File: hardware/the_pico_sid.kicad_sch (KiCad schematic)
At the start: 17 parts, among them J1 SWD, J2 Conn_01x06, U1 LM324, U2 SID_6581, U3 Pico, U4 4050, U5 4050, U6 74HC245

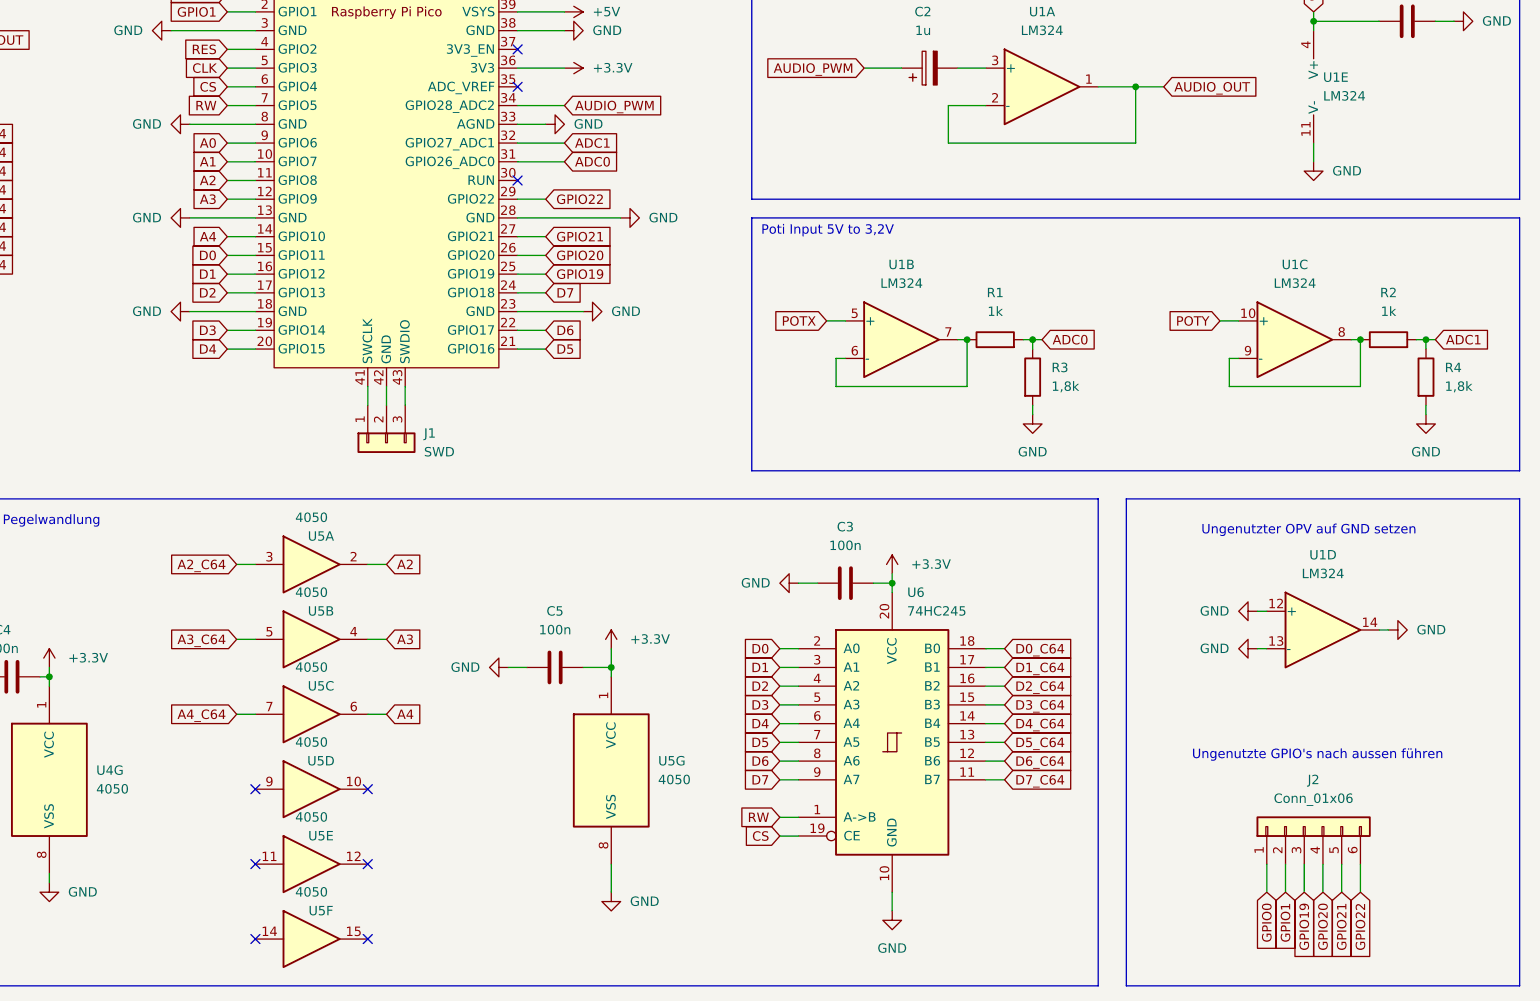
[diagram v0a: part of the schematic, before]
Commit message: schematic: changed the adc implementation
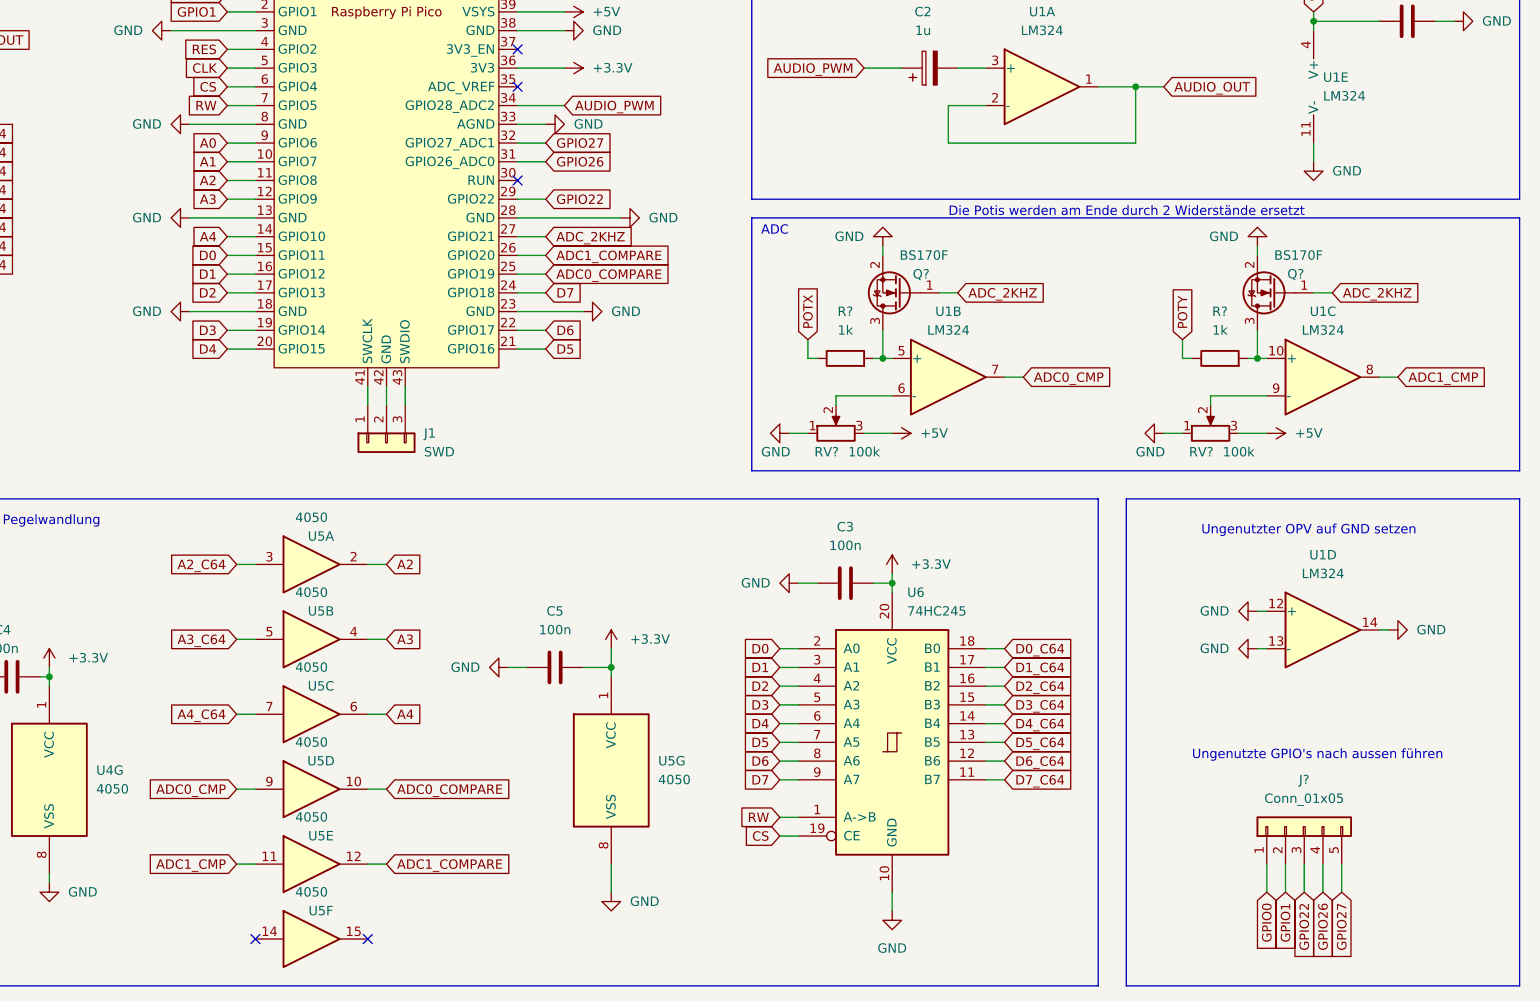
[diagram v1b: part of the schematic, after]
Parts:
- removed J2: Conn_01x06, symbol Connector_Generic:Conn_01x06
- removed R1, R2: 1k, symbol Device:R
- removed R3, R4: 1,8k, symbol Device:R
- added J?: Conn_01x05, symbol Connector_Generic:Conn_01x05
- added Q? (x2): BS170F, Package_TO_SOT_SMD:SOT-23, symbol Transistor_FET:BS170F
- added R? (x2): 1k, symbol Device:R
- added RV? (x2): 100k, symbol Device:R_Potentiometer
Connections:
- net GPIO19 is gone; now on net ADC0_COMPARE: U3.25 (GPIO19)
- net GPIO20 is gone; now on net ADC1_COMPARE: U3.26 (GPIO20)
- net +5V: now also RV?.3, RV?.3
- net GND: now also Q?.2 (S), Q?.2 (S), RV?.1, RV?.1
- net GPIO0: now also J?.1 (Pin_1)
- net GPIO1: now also J?.2 (Pin_2)
- net GPIO22: now also J?.3 (Pin_3)
- net POTX: now also R?.1; no longer U1.5 (+)
- net POTY: now also R?.1; no longer U1.10 (+)
- net ADC0_COMPARE: now reaches U5.10
- net ADC0_CMP: now reaches U5.9
- net ADC0_CMP: now also U1.7
- net at U1.6 (-): now also RV?.2; no longer U1.7
- net at U1.9 (-): now also RV?.2; no longer U1.8
- net ADC1_CMP: now reaches U5.11
- net ADC1_CMP: now also U1.8
- net ADC1_COMPARE: now reaches U5.12
- net ADC0 renamed GPIO26
- net GPIO26: now also J?.4 (Pin_4)
- net ADC1 renamed GPIO27
- net GPIO27: now also J?.5 (Pin_5)
- net GPIO21 renamed ADC_2KHZ
- net ADC_2KHZ: now also Q?.1 (G), Q?.1 (G)
- new net: Q?.3 (D), R?.2, U1.5 (+)
- new net: Q?.3 (D), R?.2, U1.10 (+)
- no-connect marks 15 -> 11
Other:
- note added: "ADC"
- note added: "Die Potis werden am Ende durch 2 Widerstände ersetzt"
- note removed: "Poti Input 5V to 3,2V"
- moved on the sheet: U1B, U1C

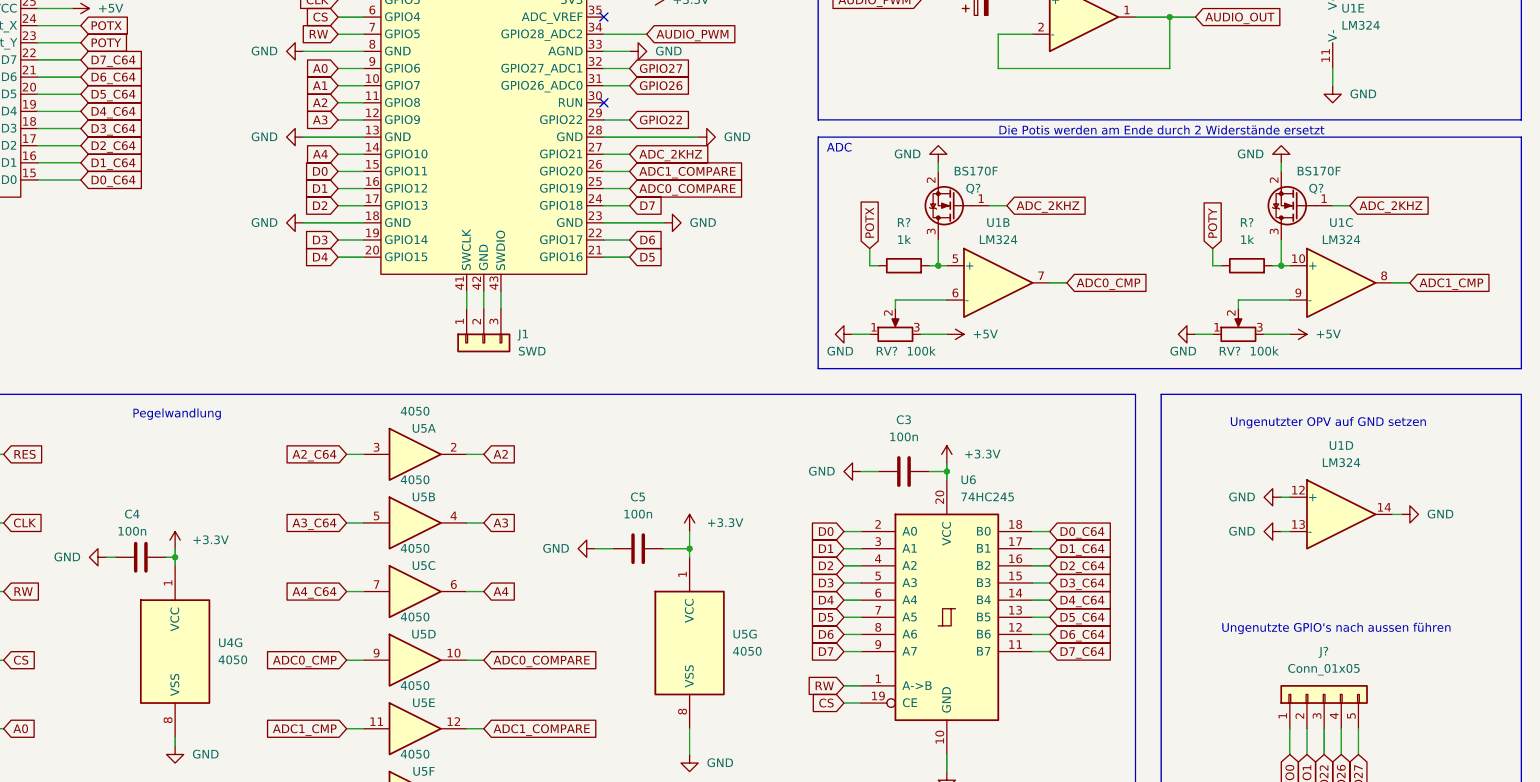
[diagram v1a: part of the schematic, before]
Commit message: schematic: replace potentiometers with constant resistors
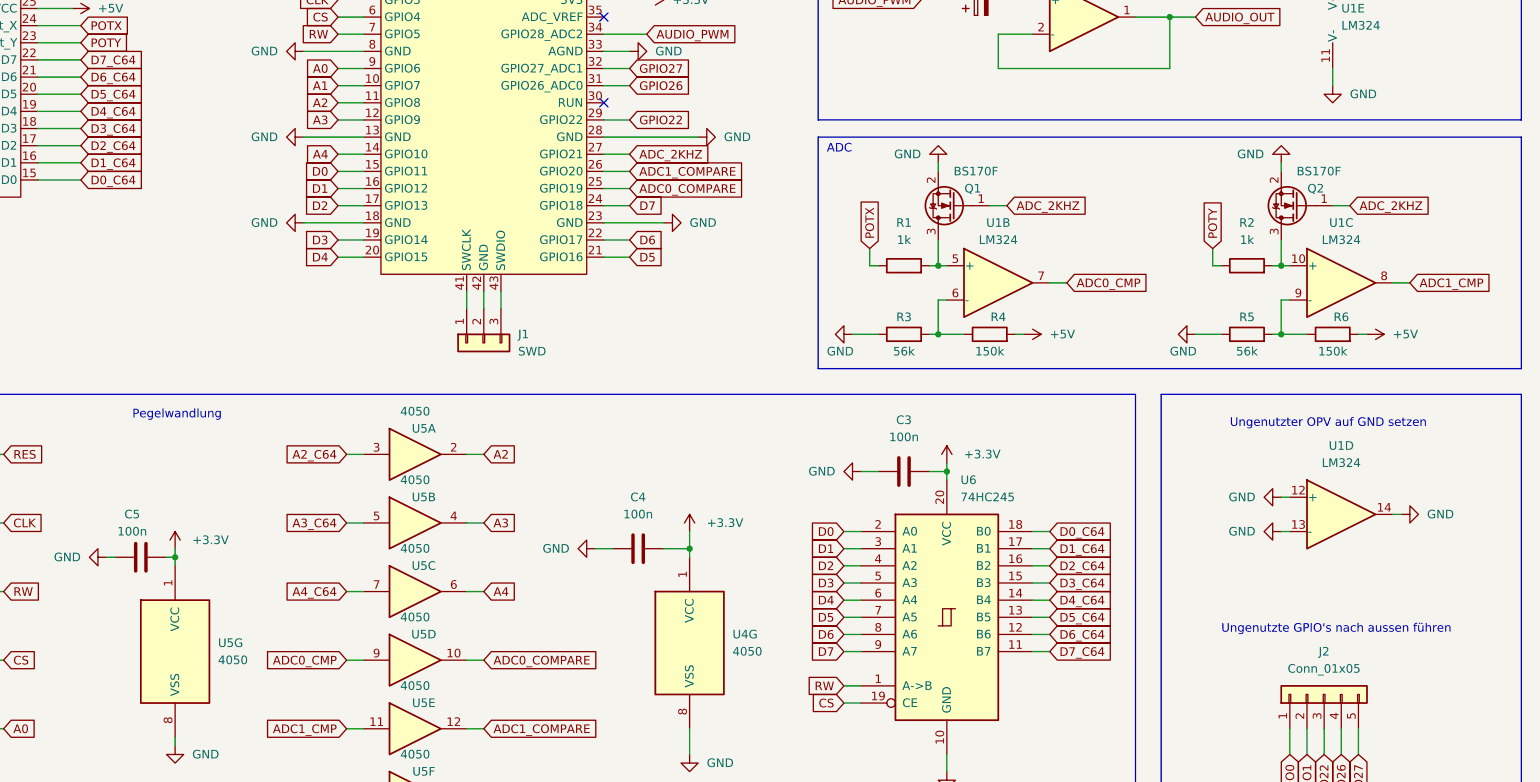
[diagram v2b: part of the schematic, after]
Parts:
- removed RV? (x2): 100k, symbol Device:R_Potentiometer
- added R3, R5: 56k, symbol Device:R
- added R4, R6: 150k, symbol Device:R
- gave numbers to parts that had none: 5
- renumbered C5 to C4, C4 to C5, U5 to U4, U4 to U5
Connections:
- net +5V: now also R4.2, R6.2
- net GND: now also R3.1, R5.1
- net at U1.6 (-): now also R3.2, R4.1
- net at U1.9 (-): now also R5.2, R6.1
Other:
- note removed: "Die Potis werden am Ende durch 2 Widerstände ersetzt"

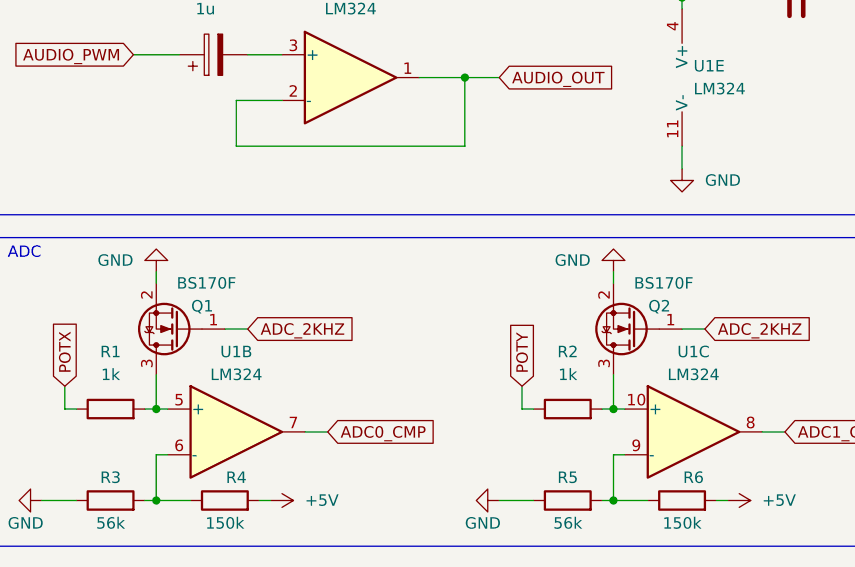
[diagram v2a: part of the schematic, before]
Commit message: shematic: mosfets swap, BS170 -> 2N7002
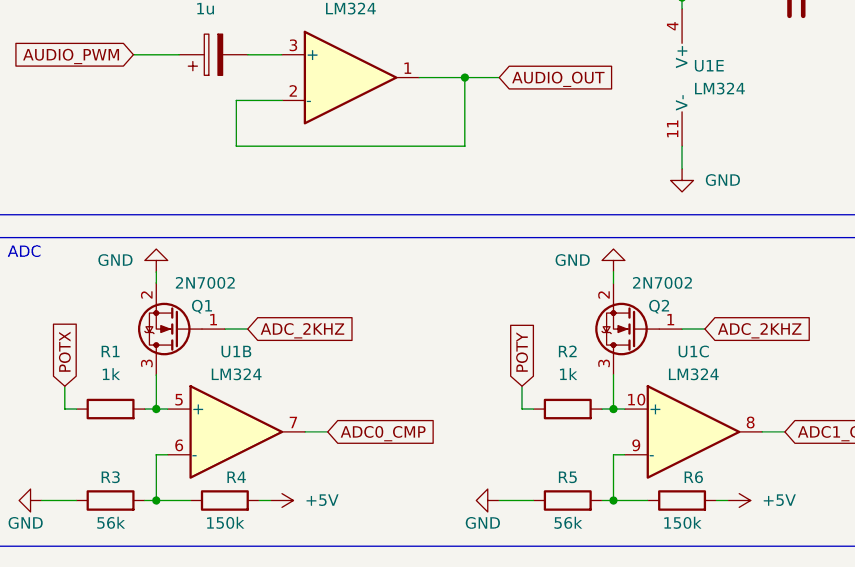
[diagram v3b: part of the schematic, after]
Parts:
- removed Q1, Q2: BS170F, Package_TO_SOT_SMD:SOT-23, symbol Transistor_FET:BS170F
- added Q1, Q2: 2N7002, Package_TO_SOT_SMD:SOT-23, symbol Transistor_FET:2N7002
- C1, C3, C4, C5: footprint (none) -> Capacitor_SMD:C_0805_2012Metric_Pad1.18x1.45mm_HandSolder
- C2: footprint (none) -> Capacitor_SMD:CP_Elec_4x4.5
- J1: footprint (none) -> Connector_PinHeader_2.54mm:PinHeader_1x03_P2.54mm_Vertical
- J2: footprint (none) -> Connector_PinHeader_2.54mm:PinHeader_1x05_P2.54mm_Vertical
- R1, R2, R3, R4, R5, R6: footprint (none) -> Resistor_SMD:R_0805_2012Metric_Pad1.20x1.40mm_HandSolder
- U1, U4, U5: footprint (none) -> Package_SO:SOIC-14_3.9x8.7mm_P1.27mm
- U6: footprint (none) -> Package_SO:SOIC-20W_7.5x12.8mm_P1.27mm
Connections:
- net ADC_2KHZ: now also Q1.1 (G), Q2.1 (G)
- net GND: now also Q1.2 (S), Q2.2 (S)
- net at R1.2, U1.5 (+): now also Q1.3 (D)
- net at R2.2, U1.10 (+): now also Q2.3 (D)

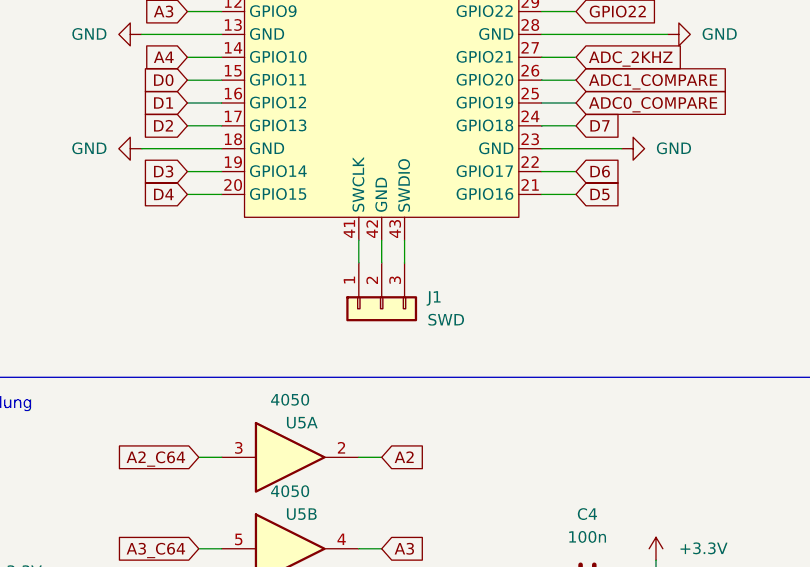
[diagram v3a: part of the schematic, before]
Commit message: schematic: change footprint for 4050 from SO14 to SO16
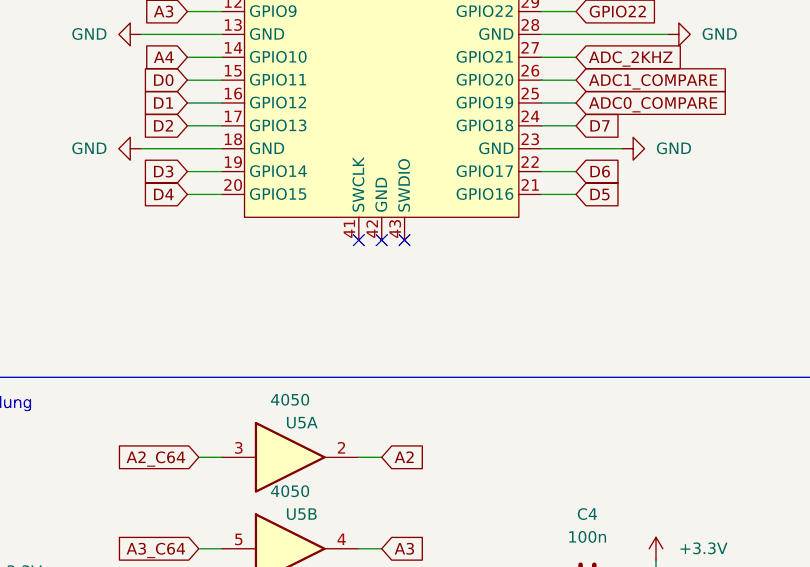
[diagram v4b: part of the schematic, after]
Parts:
- removed J1: SWD, Connector_PinHeader_2.54mm:PinHeader_1x03_P2.54mm_Vertical, symbol Connector_Generic:Conn_01x03
- U2: footprint Package_DIP:DIP-28_W15.24mm_Socket_LongPads -> c64_tk:c64_sid_pins
- U3: footprint MCU_RaspberryPi_and_Boards:RPi_Pico_SMD_TH -> connector_tk:RPi_Pico_SMD_TH
- U4, U5: footprint Package_SO:SOIC-14_3.9x8.7mm_P1.27mm -> Package_SO:SOIC-16_3.9x9.9mm_P1.27mm
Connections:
- no-connect marks 11 -> 14
